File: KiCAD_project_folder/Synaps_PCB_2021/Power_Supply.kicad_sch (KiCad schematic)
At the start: 36 parts, among them J1 USB_C_Receptacle, Q2 Q_PMOS_DGS, SW2 SW_Push, U1 MAX14748BEWW+

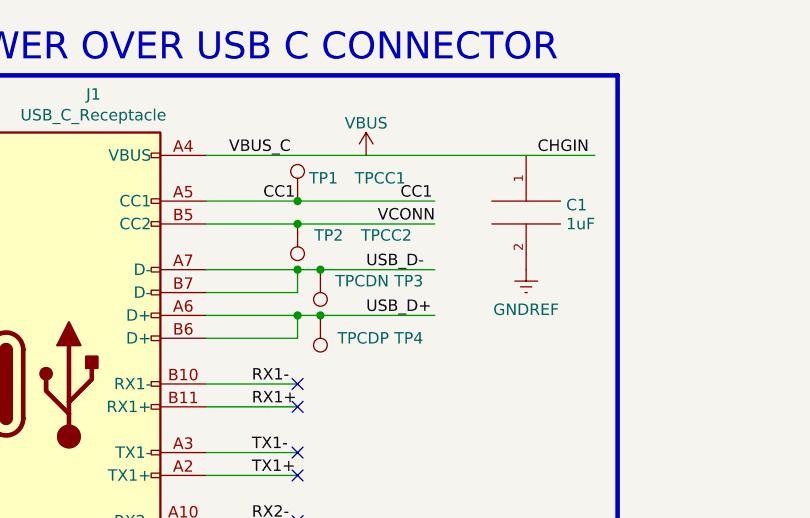
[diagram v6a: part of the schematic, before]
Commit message: Fixed missing connections + plus added rough BOM
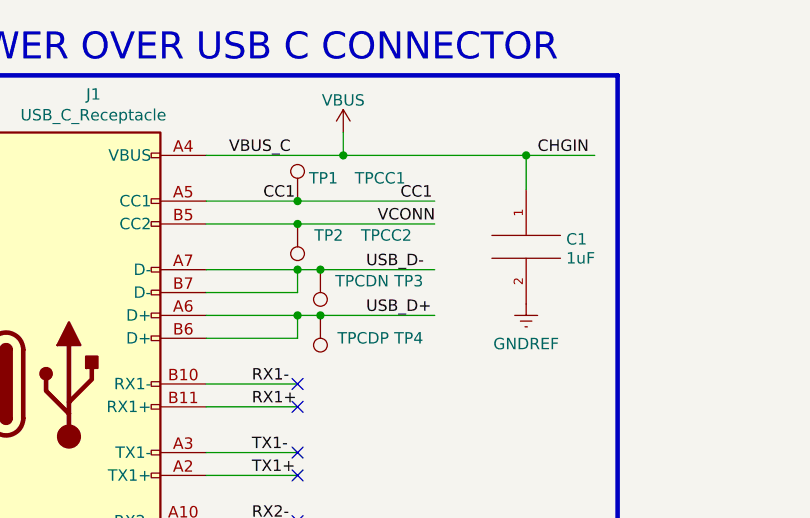
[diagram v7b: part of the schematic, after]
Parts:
- Q2: footprint Transformer_NF_ETAL_P2781 -> Transformer_SMD:Transformer_NF_ETAL_P2781
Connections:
- net CHGIN is gone; now on net VBUS: J1.A4 (VBUS), J1.A9 (VBUS), J1.B4 (VBUS), J1.B9 (VBUS)
- net VBUS: now also C1.1
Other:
- moved on the sheet: C1
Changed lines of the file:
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@@
   (junction (at 245.11 137.16) (diameter 0) (color 0 0 0 0)
   )
+  (junction (at 85.09 29.21) (diameter 0) (color 0 0 0 0)
+  )
   (junction (at 128.27 81.28) (diameter 0) (color 0 0 0 0)
   )
@@
   )
   (junction (at 254 144.78) (diameter 0) (color 0 0 0 0)
+  )
+  (junction (at 64.77 29.21) (diameter 0) (color 0 0 0 0)
   )
   (junction (at 165.1 109.22) (diameter 0) (color 0 0 0 0)
@@
     (stroke (width 0.508) (type default) (color 0 0 0 0))
   )
+  (wire (pts (xy 49.53 29.21) (xy 64.77 29.21))
+    (stroke (width 0) (type default) (color 0 0 0 0))
+  )
   (polyline (pts (xy 19.05 193.04) (xy 43.18 193.04))
     (stroke (width 0) (type default) (color 0 0 0 0))
@@
     (stroke (width 0) (type default) (color 0 0 0 0))
   )
+  (wire (pts (xy 85.09 29.21) (xy 92.71 29.21))
+    (stroke (width 0) (type default) (color 0 0 0 0))
+  )
   (polyline (pts (xy 86.36 162.56) (xy 86.36 193.04))
     (stroke (width 0) (type default) (color 0 0 0 0))
@@
     (stroke (width 0) (type default) (color 0 0 0 0))
   )
+  (wire (pts (xy 228.6 50.8) (xy 228.6 53.34))
+    (stroke (width 0) (type default) (color 0 0 0 0))
+  )
   (wire (pts (xy 165.1 58.42) (xy 165.1 60.96))
     (stroke (width 0) (type default) (color 0 0 0 0))
@@
     (stroke (width 0) (type default) (color 0 0 0 0))
   )
-  (wire (pts (xy 49.53 29.21) (xy 92.71 29.21))
-    (stroke (width 0) (type default) (color 0 0 0 0))
-  )
   (wire (pts (xy 255.905 68.58) (xy 255.905 69.85))
     (stroke (width 0) (type default) (color 0 0 0 0))
@@
     (stroke (width 0) (type default) (color 0 0 0 0))
   )
+  (wire (pts (xy 64.77 26.67) (xy 64.77 29.21))
+    (stroke (width 0) (type default) (color 0 0 0 0))
+  )
   (wire (pts (xy 160.02 96.52) (xy 165.1 96.52))
     (stroke (width 0) (type default) (color 0 0 0 0))
@@
   )
   (wire (pts (xy 254 148.59) (xy 260.35 148.59))
+    (stroke (width 0) (type default) (color 0 0 0 0))
+  )
+  (wire (pts (xy 85.09 33.02) (xy 85.09 29.21))
     (stroke (width 0) (type default) (color 0 0 0 0))
   )
@@
     (stroke (width 0) (type default) (color 0 0 0 0))
   )
+  (wire (pts (xy 64.77 29.21) (xy 85.09 29.21))
+    (stroke (width 0) (type default) (color 0 0 0 0))
+  )
   (wire (pts (xy 22.86 182.88) (xy 31.75 182.88))
     (stroke (width 0) (type default) (color 0 0 0 0))
@@
   )
   (wire (pts (xy 133.985 93.98) (xy 133.985 90.17))
-    (stroke (width 0) (type default) (color 0 0 0 0))
-  )
-  (wire (pts (xy 228.6 50.8) (xy 228.6 53.34))
     (stroke (width 0) (type default) (color 0 0 0 0))
   )
@@
     (property "Reference" "Q2" (id 0) (at 228.6 36.195 90))
     (property "Value" "Q_PMOS_DGS" (id 1) (at 228.6 38.735 90))
-    (property "Footprint" "Transformer_NF_ETAL_P2781" (id 2) (at 231.14 40.64 0)
+    (property "Footprint" "Transformer_SMD:Transformer_NF_ETAL_P2781" (id 2) (at 231.14 40.64 0)
       (effects (font (size 1.27 1.27)) hide)
     )
@@
     (pin "1")
   )
+  (symbol (lib_id "power:VBUS") (at 64.77 26.67 0) (unit 1)
+    (in_bom yes) (on_board yes) (fields_autoplaced)
+    (property "Reference" "#PWR0103" (id 0) (at 64.77 30.48 0)
+      (effects (font (size 1.27 1.27)) hide)
+    )
+    (property "Value" "VBUS" (id 1) (at 64.77 23.0942 0))
+    (property "Footprint" "" (id 2) (at 64.77 26.67 0)
+      (effects (font (size 1.27 1.27)) hide)
+    )
+    (property "Datasheet" "" (id 3) (at 64.77 26.67 0)
+      (effects (font (size 1.27 1.27)) hide)
+    )
+    (pin "1")
+  )
   (symbol (lib_id "Device:LED") (at 256.54 156.21 0) (unit 1)
     (in_bom yes) (on_board yes)
@@
     (pin "2")
   )
-  (symbol (lib_id "power:GNDREF") (at 85.09 41.91 0) (unit 1)
-    (in_bom yes) (on_board yes) (fields_autoplaced)
-    (property "Reference" "#PWR03" (id 0) (at 85.09 48.26 0)
-      (effects (font (size 1.27 1.27)) hide)
-    )
-    (property "Value" "GNDREF" (id 1) (at 85.09 46.3534 0))
-    (property "Footprint" "" (id 2) (at 85.09 41.91 0)
-      (effects (font (size 1.27 1.27)) hide)
-    )
-    (property "Datasheet" "" (id 3) (at 85.09 41.91 0)
+  (symbol (lib_id "power:GNDREF") (at 85.09 45.72 0) (unit 1)
+    (in_bom yes) (on_board yes) (fields_autoplaced)
+    (property "Reference" "#PWR03" (id 0) (at 85.09 52.07 0)
+      (effects (font (size 1.27 1.27)) hide)
+    )
+    (property "Value" "GNDREF" (id 1) (at 85.09 50.1634 0))
+    (property "Footprint" "" (id 2) (at 85.09 45.72 0)
+      (effects (font (size 1.27 1.27)) hide)
+    )
+    (property "Datasheet" "" (id 3) (at 85.09 45.72 0)
       (effects (font (size 1.27 1.27)) hide)
     )
@@
     (pin "1")
   )
-  (symbol (lib_id "pspice:CAP") (at 85.09 35.56 0) (unit 1)
-    (in_bom yes) (on_board yes)
-    (property "Reference" "C1" (id 0) (at 89.535 34.7253 0)
+  (symbol (lib_id "pspice:CAP") (at 85.09 39.37 0) (unit 1)
+    (in_bom yes) (on_board yes)
+    (property "Reference" "C1" (id 0) (at 89.535 38.5353 0)
       (effects (font (size 1.27 1.27)) (justify left))
     )
-    (property "Value" "1uF" (id 1) (at 89.535 36.83 0)
+    (property "Value" "1uF" (id 1) (at 89.535 40.64 0)
       (effects (font (size 1.27 1.27)) (justify left))
     )
-    (property "Footprint" "Capacitor_SMD:C_1206_3216Metric_Pad1.33x1.80mm_HandSolder" (id 2) (at 85.09 35.56 0)
-      (effects (font (size 1.27 1.27)) hide)
-    )
-    (property "Datasheet" "~" (id 3) (at 85.09 35.56 0)
+    (property "Footprint" "Capacitor_SMD:C_1206_3216Metric_Pad1.33x1.80mm_HandSolder" (id 2) (at 85.09 39.37 0)
+      (effects (font (size 1.27 1.27)) hide)
+    )
+    (property "Datasheet" "~" (id 3) (at 85.09 39.37 0)
       (effects (font (size 1.27 1.27)) hide)
     )
@@
       (effects (font (size 1.27 1.27)) hide)
     )
-    (pin "1")
-  )
-  (symbol (lib_id "power:VBUS") (at 67.31 29.21 0) (unit 1)
-    (in_bom yes) (on_board yes) (fields_autoplaced)
-    (property "Reference" "#PWR014" (id 0) (at 67.31 33.02 0)
-      (effects (font (size 1.27 1.27)) hide)
-    )
-    (property "Value" "VBUS" (id 1) (at 67.31 25.6342 0))
-    (property "Footprint" "" (id 2) (at 67.31 29.21 0)
-      (effects (font (size 1.27 1.27)) hide)
-    )
-    (property "Datasheet" "" (id 3) (at 67.31 29.21 0)
-      (effects (font (size 1.27 1.27)) hide)
-    )

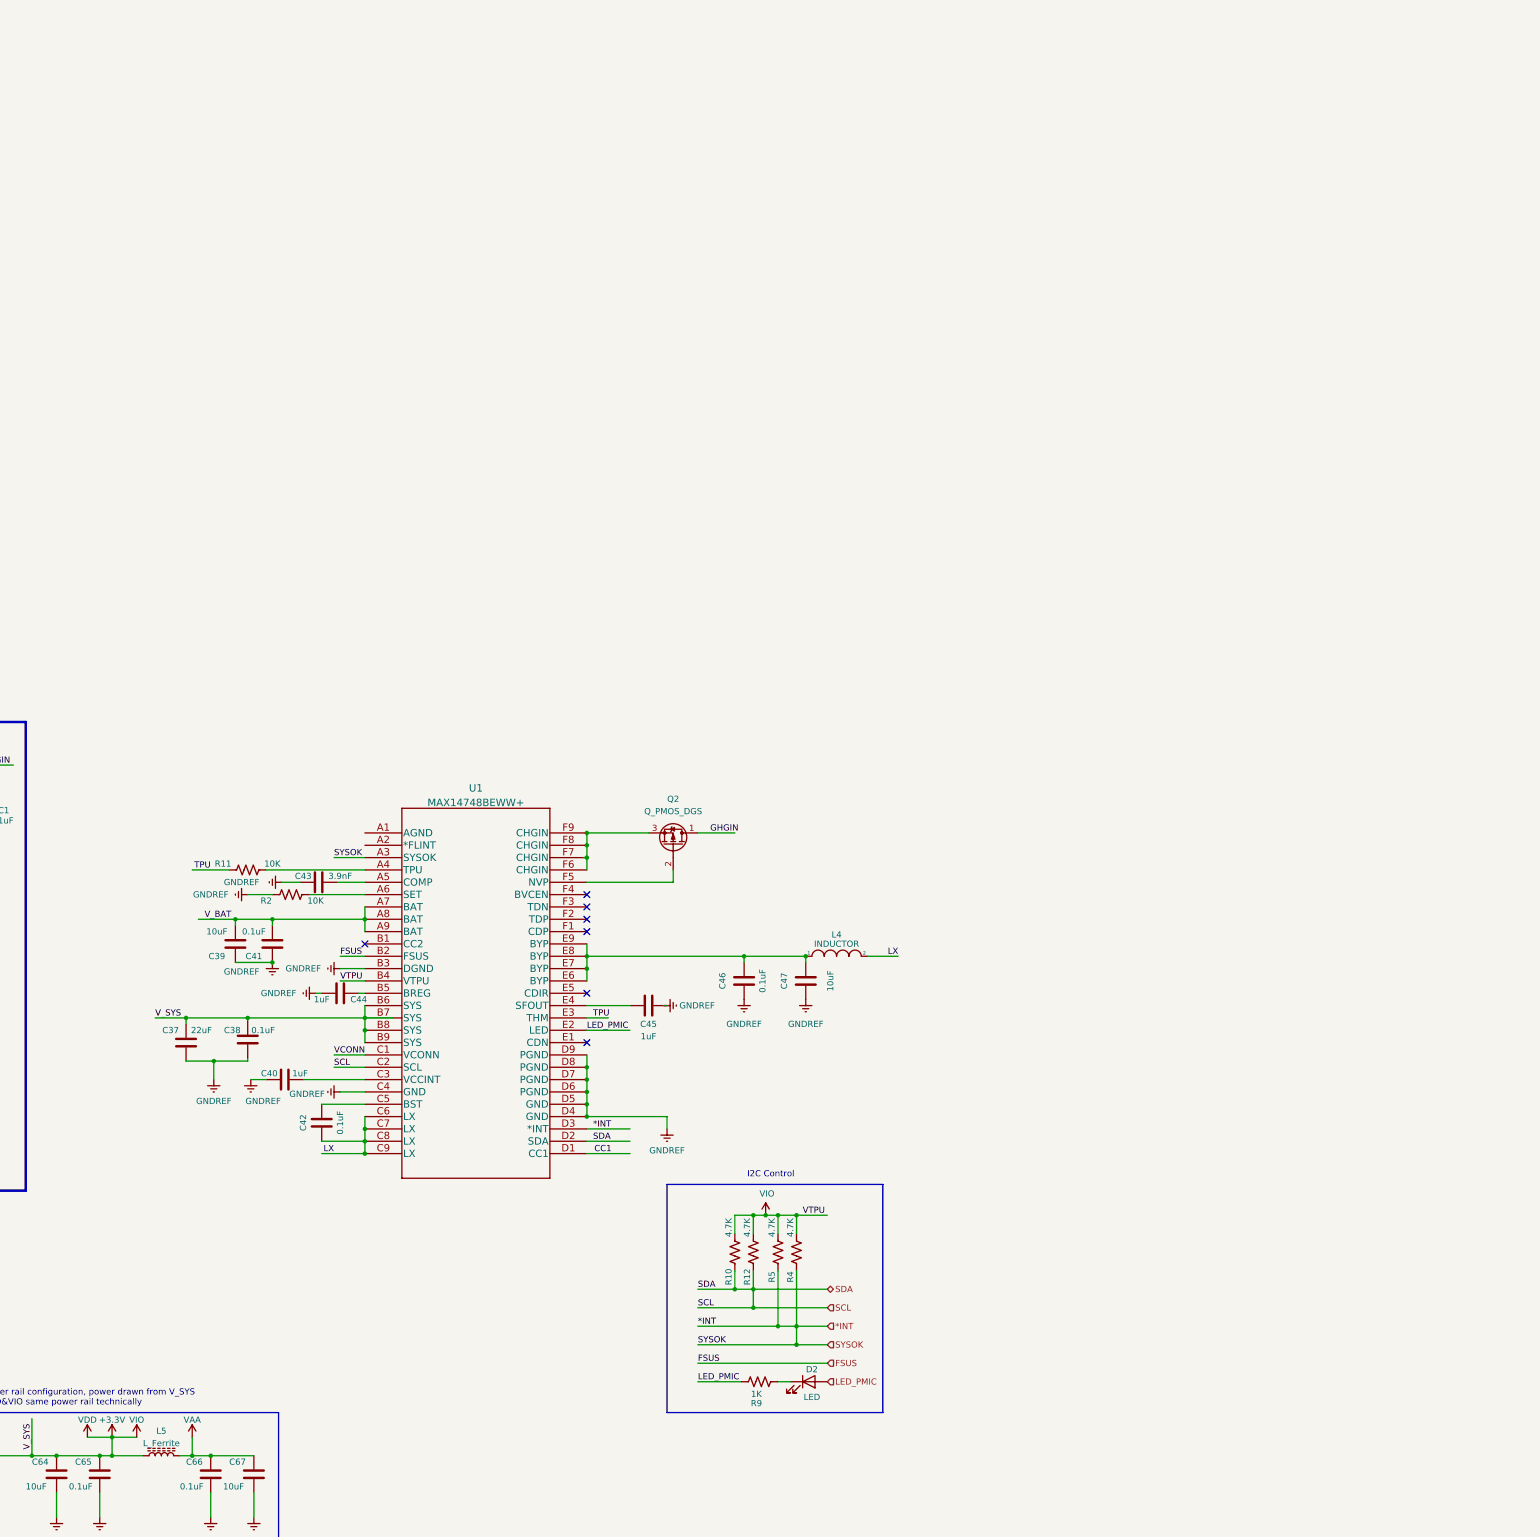
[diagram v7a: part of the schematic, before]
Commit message: Updated BOM and power circuit has to be redone because of missing parts
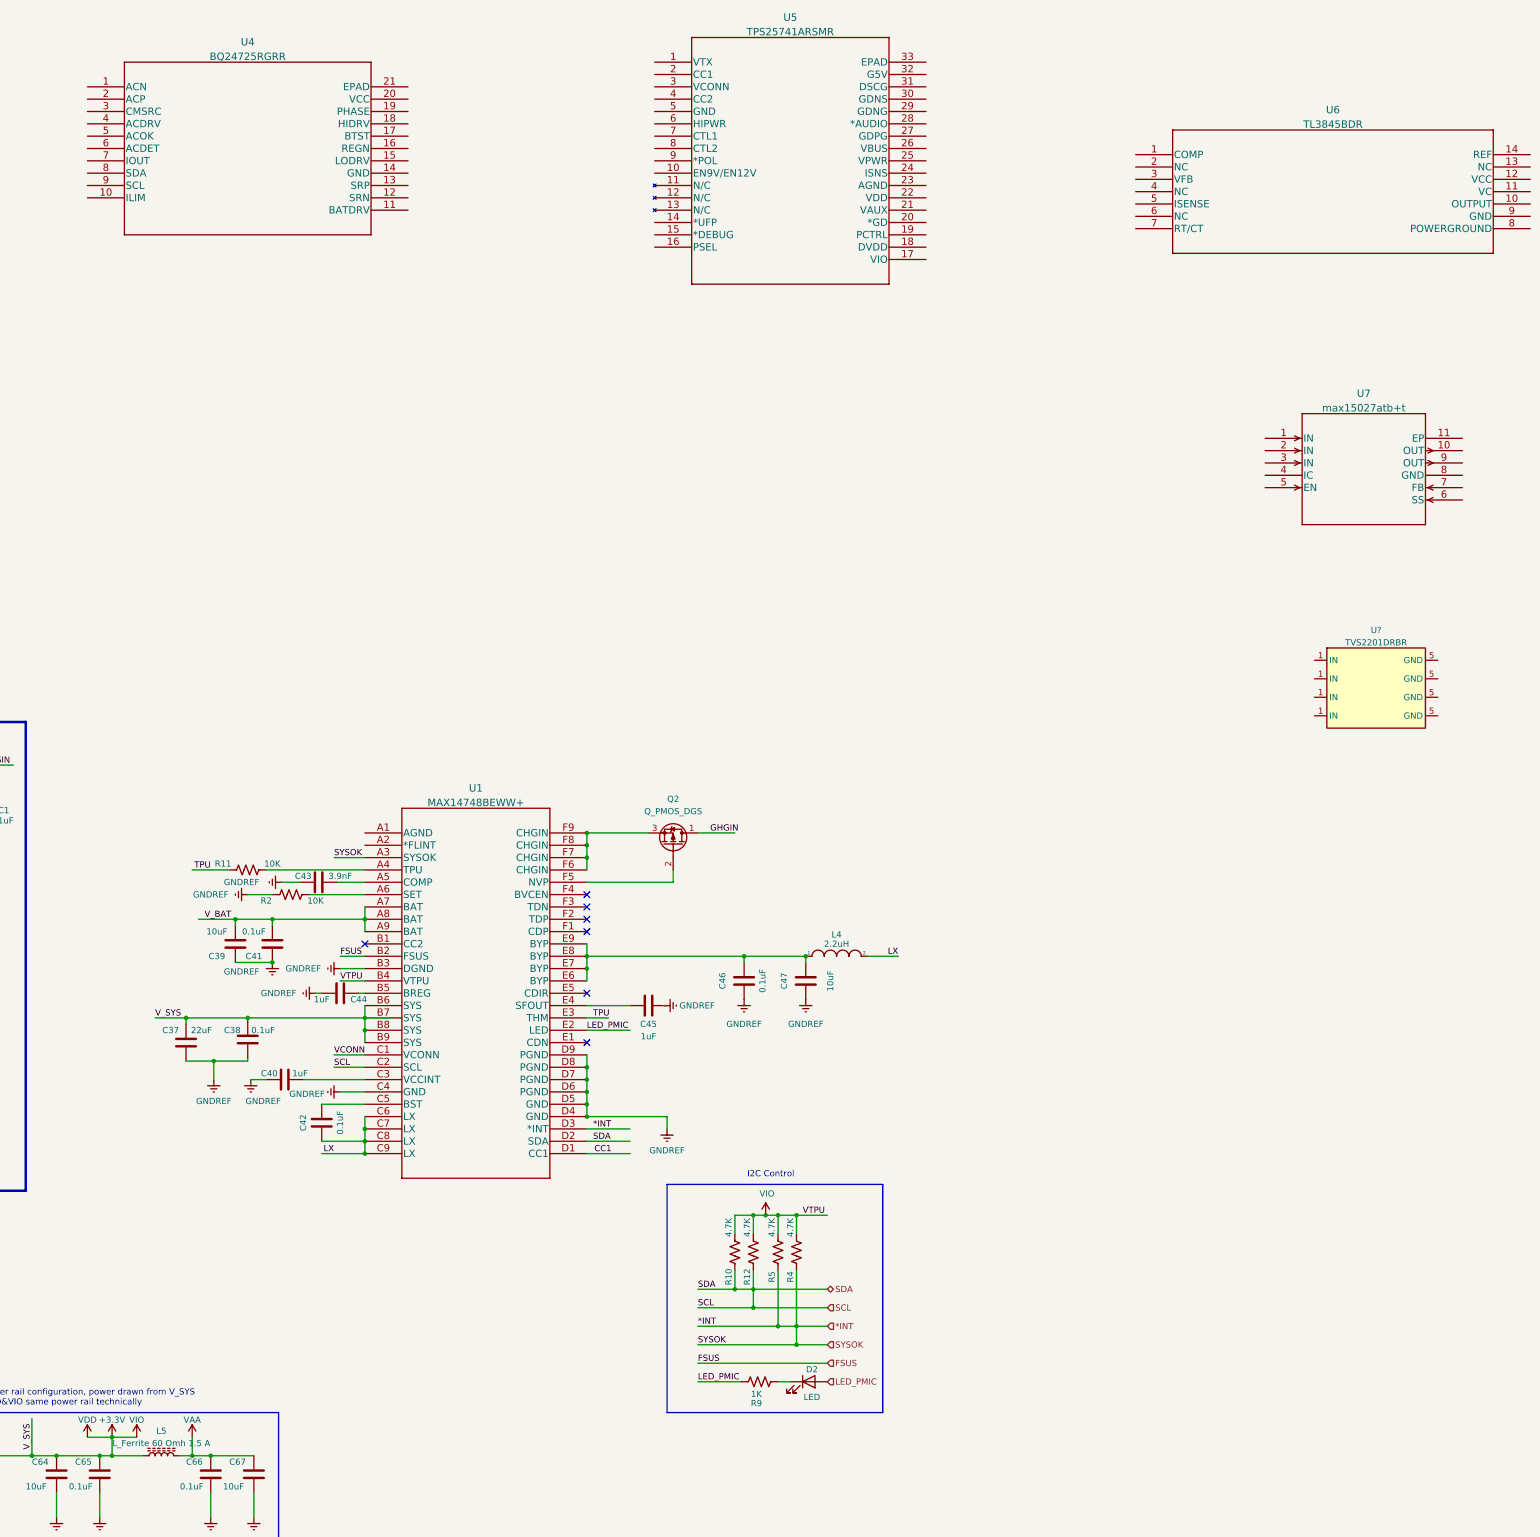
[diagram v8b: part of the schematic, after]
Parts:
- added U4: BQ24725RGRR, BQ24725:BQ24725RGRR, symbol BQ24725:BQ24725RGRR
- added U5: TPS25741ARSMR, TPS25741:TPS25741ARSMR, symbol TPS25741:TPS25741ARSMR
- added U6: TL3845BDR, TL3845BDR:TL3845BDR, symbol TL3845BDR:TL3845BDR
- added U7: max15027atb+t, MAX15027:max15027atb&plus_t, symbol MAX15027:max15027atb+t
- added U?: TVS2201DRBR, TVS2201:IC_DRV8601DRBT, symbol TVS2201:TVS2201DRBR
- C1, C40, C44, C45: MPN (none) -> GCM31MR71H105KA55L; Supplier Link (none) -> https://www.digikey.ca/en/products/detail/murata-electronic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
- C37: MPN (none) -> CL31B226MPHNNNE; Supplier Link (none) -> https://www.digikey.ca/en/products/detail/samsung-electro-m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
- C38, C41, C42, C46, C65, C66: MPN (none) -> CC1206KRX7R9BB104; Supplier Link (none) -> https://www.digikey.ca/en/products/detail/yageo/CC1206KRX7R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
- C39, C47, C64, C67: MPN (none) -> CL31B106KAHNNNE; Supplier Link (none) -> https://www.digikey.ca/en/products/detail/samsung-electro-m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
- C43: MPN (none) -> C1206C392KDRAC7800; Supplier Link (none) -> https://www.digikey.ca/en/products/detail/kemet/C1206C392KD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
- D2: MPN (none) -> LTST-C190KGKT; Supplier Link (none) -> https://www.digikey.ca/en/products/detail/liteon/LTST-C190K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
- J1: MPN (none) -> USB4085-GF-A; Supplier Link (none) -> https://www.digikey.ca/en/products/detail/gct/USB4085-GF-A/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
- L4: value INDUCTOR -> 2.2uH; MPN (none) -> NRS6028T2R2NMGJ; Supplier Link (none) -> https://www.digikey.ca/en/products/detail/taiyo-yuden/NRS60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
- L5: value L_Ferrite -> L_Ferrite 60 Omh 1.5 A; MPN (none) -> MPZ1005S600CT000; Supplier Link (none) -> https://www.digikey.ca/en/products/detail/tdk-corporation/M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
- R10, R12, R4, R5: MPN (none) -> RC1206FR-074K7L; Supplier Link (none) -> https://www.digikey.ca/en/products/detail/yageo/RC1206FR-07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
- R11, R2: MPN (none) -> RC1206JR-0710KL; Supplier Link (none) -> https://www.digikey.ca/en/products/detail/yageo/RC1206JR-07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
- R3: MPN (none) -> RC1206FR-071ML; Supplier Link (none) -> https://www.digikey.ca/en/products/detail/yageo/RC1206FR-07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
- R9: MPN (none) -> RNCP1206FTD1K00; Supplier Link (none) -> https://www.digikey.ca/en/products/detail/stackpole-electro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
- SW2: footprint Button_Switch_SMD:SW_Push_1P1T_NO_6x6mm_H9.5mm -> Push_Button:GPTS203211B; MPN (none) -> GPTS203211B; Supplier Link (none) -> https://www.digikey.ca/en/products/detail/cw-industries/GPT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
